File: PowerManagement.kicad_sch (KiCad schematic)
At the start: 22 parts, among them J5 Screw_Terminal_01x02_POWER, U2 XC6210B332MR, U3 XL1509

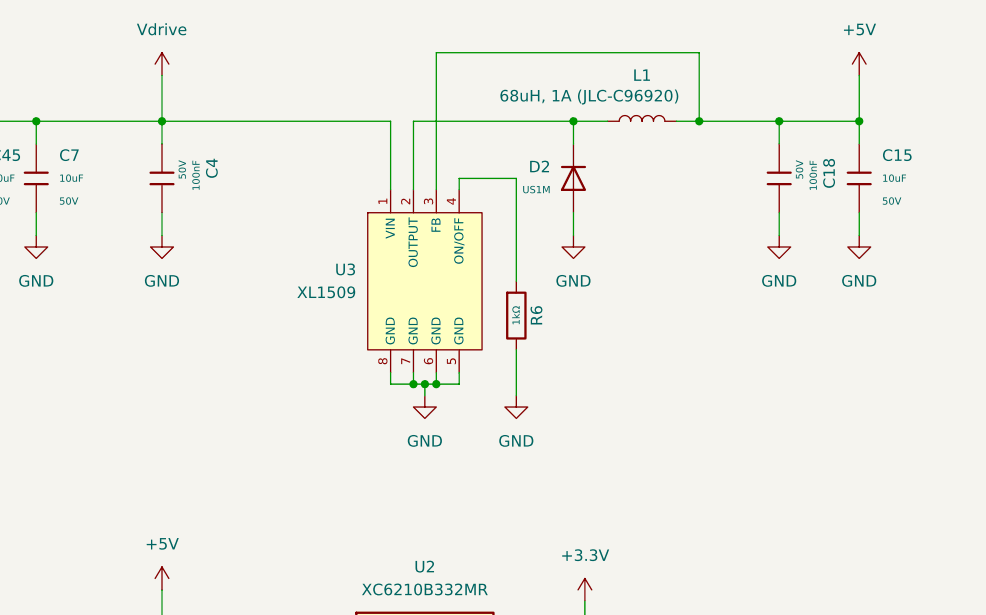
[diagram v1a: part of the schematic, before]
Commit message: added drv8353, stm32h723vgt6
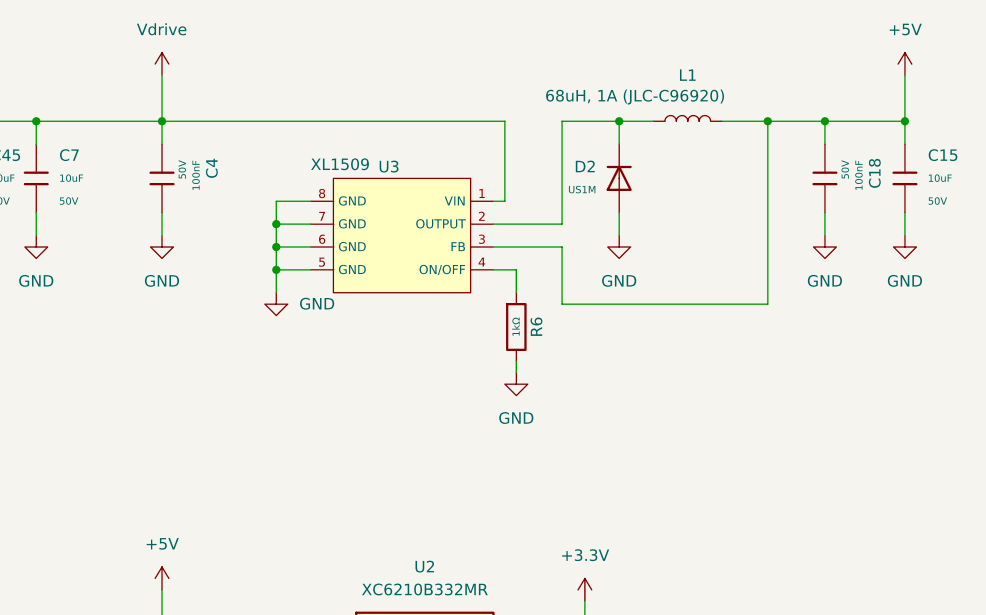
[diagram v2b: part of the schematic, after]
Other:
- moved on the sheet: C15, C18, D2, L1, R6, U3
